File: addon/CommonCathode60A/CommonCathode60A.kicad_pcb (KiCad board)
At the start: 4 copper layers, 153 x 114 mm, 18 parts, among them J101 Conn_02x20_Odd_Even Header, J102 TBL008V-1000-08BE, J103 TBL008V-1000-08BE, K101 EW60-1A3-CL12D04, K102 EW60-1A3-CL12D04, K103 EW60-1A3-CL12D04, K104 EW60-1A3-CL12D04, K105 EW60-1A3-CL12D04, K106 EW60-1A3-CL12D04, K107 EW60-1A3-CL12D04, K108 EW60-1A3-CL12D04

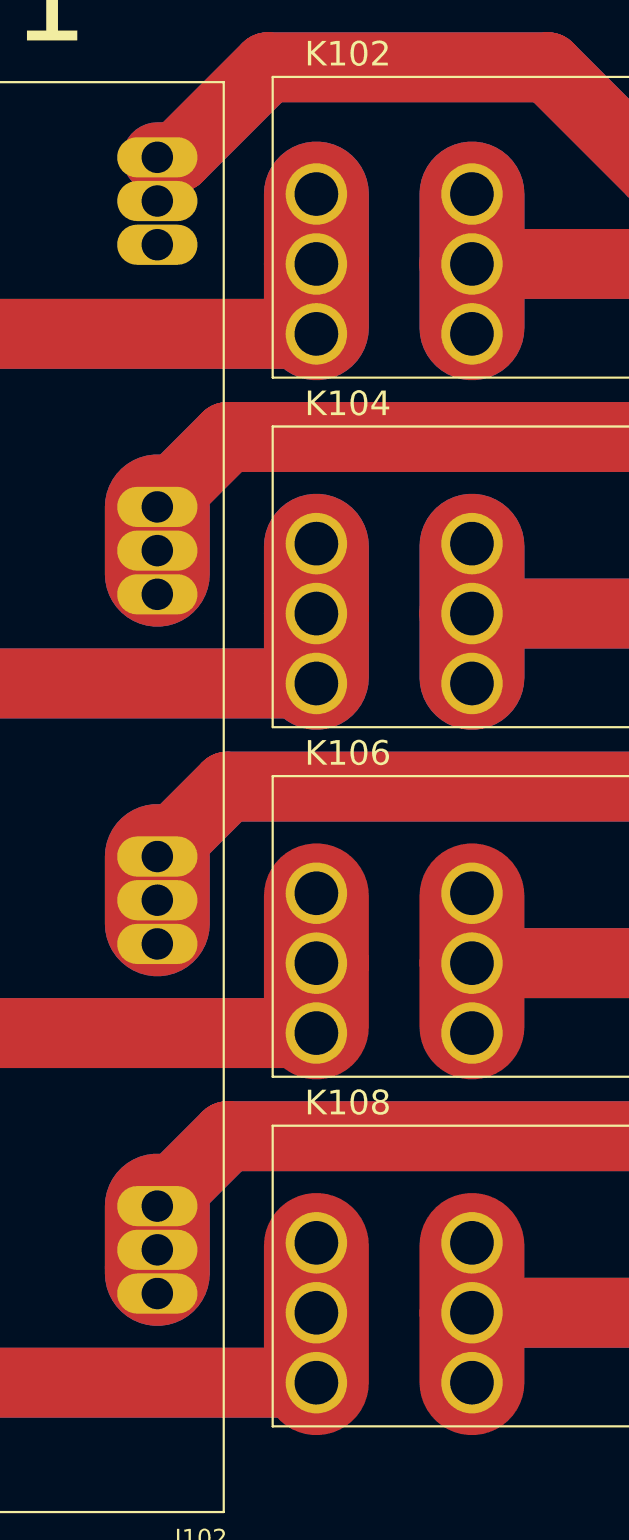
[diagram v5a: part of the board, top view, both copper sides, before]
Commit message: Wrap up non-latching
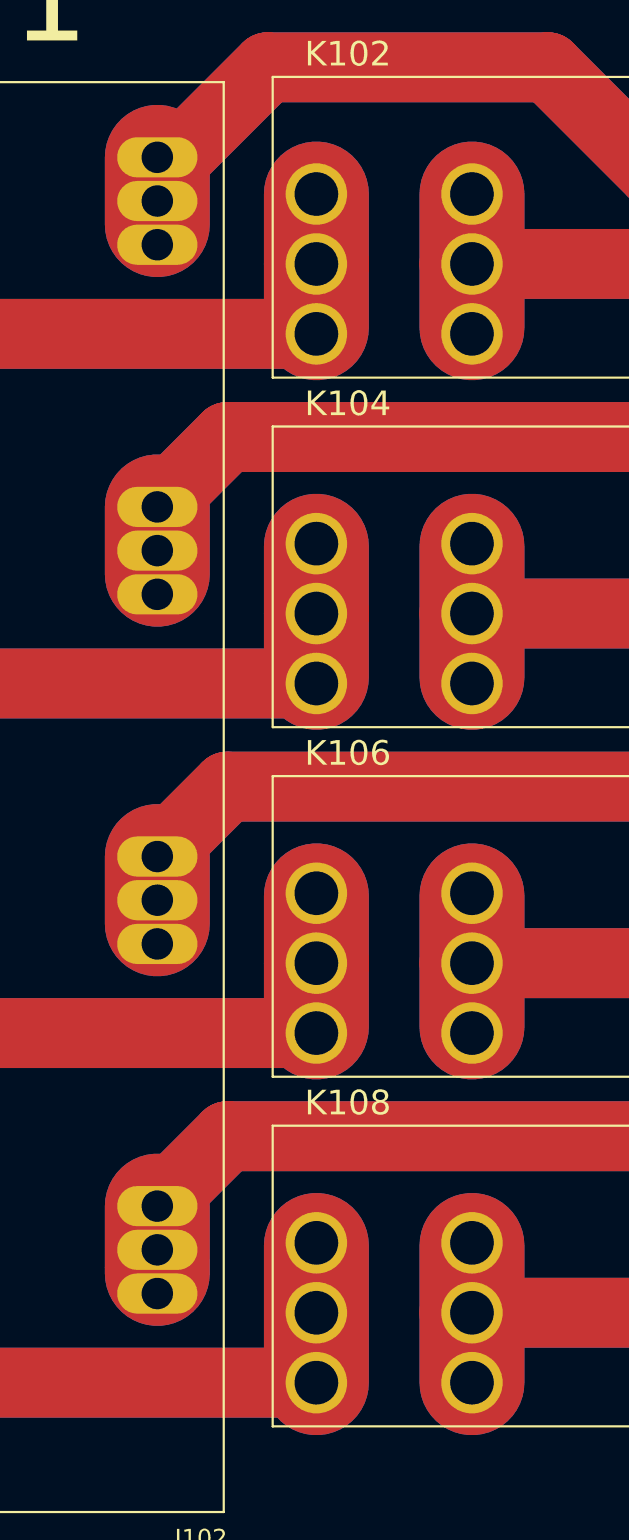
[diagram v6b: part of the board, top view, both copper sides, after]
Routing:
- net GND: track 205.5 -> 252.1 mm
- net /K1_IN: track 200.1 -> 206.7 mm
- net /K6_OUT: track 205.9 -> 205.4 mm
- net /K6_IN: track 74.7 -> 74.2 mm
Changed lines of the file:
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@@
     (thickness 1.6)
     (drawings 76)
-    (tracks 324)
+    (tracks 337)
     (zones 0)
     (modules 18)
@@
   (segment (start 110.08 37.6) (end 110.08 40.14) (width 1) (layer In2.Cu) (net 1))
   (segment (start 107.54 37.6) (end 107.54 40.14) (width 1) (layer In2.Cu) (net 1))
-  (segment (start 105 40.14) (end 112.62 40.14) (width 1) (layer In1.Cu) (net 1))
   (segment (start 112.62 40.14) (end 112.62 37.6) (width 1) (layer In1.Cu) (net 1))
   (segment (start 112.62 37.6) (end 105 37.6) (width 1) (layer In1.Cu) (net 1))
@@
   (segment (start 107.54 37.6) (end 107.54 40.14) (width 1) (layer In1.Cu) (net 1))
   (segment (start 110.08 37.6) (end 110.08 40.14) (width 1) (layer In1.Cu) (net 1))
-  (segment (start 108.7 120.3) (end 108.7 100.3) (width 1) (layer In2.Cu) (net 1))
-  (segment (start 144.3 107.7) (end 144.3 87.7) (width 1) (layer In2.Cu) (net 1))
-  (segment (start 144.3 87.7) (end 144.3 67.7) (width 1) (layer In2.Cu) (net 1))
-  (segment (start 144.3 67.7) (end 144.3 47.7) (width 1) (layer In2.Cu) (net 1))
-  (segment (start 108.7 79.027208) (end 108.7 60.3) (width 1) (layer In1.Cu) (net 1))
   (segment (start 108.7 80.3) (end 108.7 79.027208) (width 1) (layer In1.Cu) (net 1))
   (segment (start 108.7 41.3) (end 107.54 40.14) (width 1) (layer In1.Cu) (net 1))
-  (segment (start 108.7 60.3) (end 108.7 41.3) (width 1) (layer In1.Cu) (net 1))
   (segment (start 108.92 41.3) (end 110.08 40.14) (width 1) (layer In1.Cu) (net 1))
   (segment (start 108.7 41.3) (end 108.92 41.3) (width 1) (layer In1.Cu) (net 1))
-  (segment (start 107.800001 101.199999) (end 108.7 100.3) (width 1) (layer In2.Cu) (net 1))
-  (segment (start 106.699999 102.300001) (end 107.800001 101.199999) (width 1) (layer In2.Cu) (net 1))
-  (segment (start 102.659999 102.300001) (end 106.699999 102.300001) (width 1) (layer In2.Cu) (net 1))
-  (segment (start 101.619999 101.260001) (end 102.659999 102.300001) (width 1) (layer In2.Cu) (net 1))
-  (segment (start 101.619999 87.380001) (end 101.619999 101.260001) (width 1) (layer In2.Cu) (net 1))
-  (segment (start 108.7 80.3) (end 101.619999 87.380001) (width 1) (layer In2.Cu) (net 1))
+  (segment (start 108.7 40.3) (end 108.7 60.3) (width 2) (layer In1.Cu) (net 1))
+  (segment (start 108.86 40.14) (end 108.7 40.3) (width 2) (layer In1.Cu) (net 1))
+  (segment (start 105 40.14) (end 108.86 40.14) (width 1) (layer In1.Cu) (net 1))
+  (segment (start 108.86 40.14) (end 112.62 40.14) (width 1) (layer In1.Cu) (net 1))
+  (segment (start 108.7 60.3) (end 108.7 80.199991) (width 2) (layer In1.Cu) (net 1))
+  (segment (start 107.800001 101.199999) (end 108.7 100.3) (width 2) (layer In2.Cu) (net 1))
+  (segment (start 101.119999 101.500001) (end 102.419999 102.800001) (width 2) (layer In2.Cu) (net 1))
+  (segment (start 101.119999 87.880001) (end 101.119999 101.500001) (width 2) (layer In2.Cu) (net 1))
+  (segment (start 106.199999 102.800001) (end 107.800001 101.199999) (width 2) (layer In2.Cu) (net 1))
+  (segment (start 102.419999 102.800001) (end 106.199999 102.800001) (width 2) (layer In2.Cu) (net 1))
+  (segment (start 108.7 80.3) (end 101.119999 87.880001) (width 2) (layer In2.Cu) (net 1))
+  (segment (start 108.7 100.3) (end 108.7 120.3) (width 2) (layer In2.Cu) (net 1))
+  (segment (start 144.3 48.972792) (end 144.3 67.7) (width 2) (layer In2.Cu) (net 1))
+  (segment (start 144.3 47.7) (end 144.3 48.972792) (width 2) (layer In2.Cu) (net 1))
+  (segment (start 144.3 68.972792) (end 144.3 87.7) (width 2) (layer In2.Cu) (net 1))
+  (segment (start 144.3 67.7) (end 144.3 68.972792) (width 2) (layer In2.Cu) (net 1))
+  (segment (start 144.3 88.972792) (end 144.3 107.7) (width 2) (layer In2.Cu) (net 1))
+  (segment (start 144.3 87.7) (end 144.3 88.972792) (width 2) (layer In2.Cu) (net 1))
+  (segment (start 143.400001 108.599999) (end 144.3 107.7) (width 2) (layer In1.Cu) (net 1))
+  (segment (start 129.199999 122.800001) (end 143.400001 108.599999) (width 2) (layer In1.Cu) (net 1))
+  (segment (start 111.200001 122.800001) (end 129.199999 122.800001) (width 2) (layer In1.Cu) (net 1))
+  (segment (start 108.7 120.3) (end 111.200001 122.800001) (width 2) (layer In1.Cu) (net 1))
   (segment (start 117.7 116.3) (end 113.7 120.3) (width 1) (layer In1.Cu) (net 2))
   (segment (start 117.7 40.14) (end 117.7 116.3) (width 1) (layer In1.Cu) (net 2))
@@
   (segment (start 83.1 76.1) (end 83.1 79.74999) (width 6) (layer F.Cu) (net 15))
   (segment (start 83.1 76.1) (end 83.1 72.25001) (width 6) (layer F.Cu) (net 15))
-  (segment (start 83.1 112.1) (end 83.1 120.1) (width 4) (layer B.Cu) (net 16))
   (segment (start 61.4 120.1) (end 59 122.5) (width 4) (layer B.Cu) (net 16))
   (segment (start 83.1 120.1) (end 61.4 120.1) (width 4) (layer B.Cu) (net 16))
@@
   (segment (start 59 125) (end 59 120) (width 8) (layer B.Cu) (net 16))
   (segment (start 83.1 120.1) (end 83.1 112.25001) (width 6) (layer F.Cu) (net 16))
+  (segment (start 83.1 120.1) (end 83.1 112.25001) (width 6) (layer B.Cu) (net 16))
   (segment (start 74 70) (end 78 66) (width 4) (layer F.Cu) (net 17))
   (segment (start 78 66) (end 129.5 66) (width 4) (layer F.Cu) (net 17))
@@
   (segment (start 83.1 56.1) (end 83.1 59.74999) (width 6) (layer F.Cu) (net 19))
   (segment (start 83.1 56.1) (end 83.1 52.1) (width 6) (layer F.Cu) (net 19))
-  (segment (start 83.1 92.1) (end 83.1 100.1) (width 4) (layer B.Cu) (net 20))
   (segment (start 61.4 100.1) (end 59 102.5) (width 4) (layer B.Cu) (net 20))
   (segment (start 83.1 100.1) (end 61.4 100.1) (width 4) (layer B.Cu) (net 20))
@@
   (segment (start 83.1 96.1) (end 83.1 99.74999) (width 6) (layer F.Cu) (net 20))
   (segment (start 83.1 96.1) (end 83.1 92.25001) (width 6) (layer F.Cu) (net 20))
+  (segment (start 83.1 96.1) (end 83.1 92.25001) (width 6) (layer B.Cu) (net 20))
+  (segment (start 83.1 96.1) (end 83.1 99.74999) (width 6) (layer B.Cu) (net 20))
   (segment (start 80.3 44.85) (end 75.15 50) (width 4) (layer F.Cu) (net 21))
   (segment (start 96.35 44.85) (end 80.3 44.85) (width 4) (layer F.Cu) (net 21))
@@
   (segment (start 130.34999 50.84999) (end 102.34999 50.84999) (width 4) (layer F.Cu) (net 21))
   (segment (start 131.350001 51.850001) (end 130.34999 50.84999) (width 4) (layer F.Cu) (net 21))
-  (segment (start 75.15 50) (end 74 50) (width 4) (layer F.Cu) (net 21))
   (segment (start 160.950001 51.850001) (end 131.350001 51.850001) (width 4) (layer F.Cu) (net 21))
   (segment (start 161 51.9) (end 160.950001 51.850001) (width 4) (layer F.Cu) (net 21))
@@
   (segment (start 161 51.9) (end 161 47.9) (width 6) (layer F.Cu) (net 21))
   (segment (start 161 51.9) (end 161 55.9) (width 6) (layer F.Cu) (net 21))
+  (segment (start 74 50) (end 74 53.84999) (width 6) (layer F.Cu) (net 21))
+  (segment (start 74 50) (end 74 53.84999) (width 6) (layer B.Cu) (net 21))
   (segment (start 135.4 91.9) (end 161 91.9) (width 4) (layer F.Cu) (net 22))
   (segment (start 129.5 86) (end 135.4 91.9) (width 4) (layer F.Cu) (net 22))
@@
   (segment (start 127.1 116.1) (end 92 116.1) (width 4) (layer B.Cu) (net 24))
   (segment (start 133.5 122.5) (end 127.1 116.1) (width 4) (layer B.Cu) (net 24))
-  (segment (start 92 112.1) (end 92 120.1) (width 4) (layer B.Cu) (net 24))
   (segment (start 92 116.1) (end 127.1 116.1) (width 4) (layer F.Cu) (net 24))
   (segment (start 133.5 122.5) (end 181 122.5) (width 4) (layer F.Cu) (net 24))
@@
   (segment (start 92 116.1) (end 92 112.25001) (width 6) (layer F.Cu) (net 24))
   (segment (start 92 116.1) (end 92 120.1) (width 6) (layer F.Cu) (net 24))
+  (segment (start 92 116.1) (end 92 112.25001) (width 6) (layer B.Cu) (net 24))
+  (segment (start 92 116.1) (end 92 120.1) (width 6) (layer B.Cu) (net 24))
   (segment (start 170.5 72.5) (end 169.9 71.9) (width 8) (layer F.Cu) (net 25))
   (segment (start 196 72.5) (end 170.5 72.5) (width 8) (layer F.Cu) (net 25))
@@
   (segment (start 92 56.1) (end 92 52.1) (width 6) (layer F.Cu) (net 27))
   (segment (start 92 56.1) (end 92 59.74999) (width 6) (layer F.Cu) (net 27))
-  (segment (start 92 92.1) (end 92 100.1) (width 4) (layer B.Cu) (net 28))
   (segment (start 181 102.5) (end 134 102.5) (width 4) (layer B.Cu) (net 28))
   (segment (start 127.6 96.1) (end 92 96.1) (width 4) (layer B.Cu) (net 28))
@@
   (segment (start 92 96.1) (end 92 92.25001) (width 6) (layer F.Cu) (net 28))
   (segment (start 92 96.1) (end 92 99.74999) (width 6) (layer F.Cu) (net 28))
+  (segment (start 92 96.1) (end 92 92.25001) (width 6) (layer B.Cu) (net 28))
+  (segment (start 92 96.1) (end 92 99.74999) (width 6) (layer B.Cu) (net 28))
   (segment (start 170.5 52.5) (end 169.9 51.9) (width 8) (layer F.Cu) (net 29))
   (segment (start 196 52.5) (end 170.5 52.5) (width 8) (layer F.Cu) (net 29))
